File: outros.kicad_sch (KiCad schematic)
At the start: 9 parts

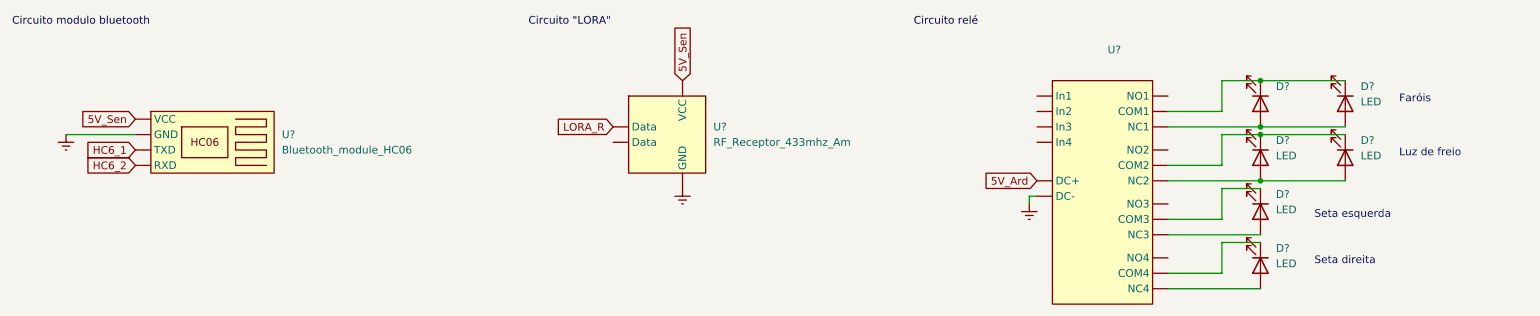
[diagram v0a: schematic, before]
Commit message: fix: modificado saídas do arduino
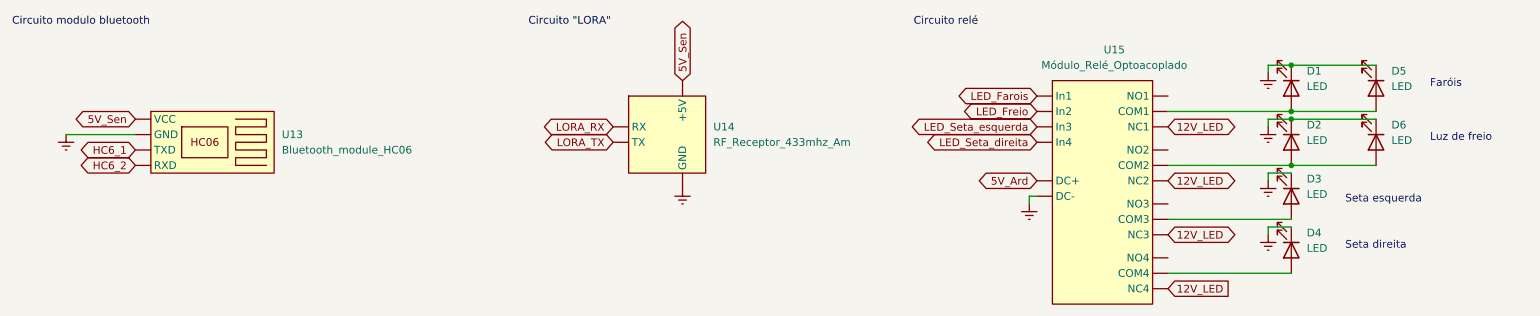
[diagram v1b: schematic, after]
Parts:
- D1: renamed from D?; value (none) -> LED
- U13: renamed from U?; footprint (none) -> Connector_PinHeader_2.54mm:PinHeader_1x04_P2.54mm_Vertical
- U14: renamed from U?; footprint (none) -> Connector_PinHeader_2.54mm:PinHeader_1x06_P2.54mm_Vertical; symbol Customizados:RF_Receptor_433mhz_Am -> Customizados:RF_Receptor_e_transmissor_915mhz
- U15: renamed from U?; value (none) -> Módulo_Relé_Optoacoplado; footprint (none) -> TerminalBlock_Phoenix:TerminalBlock_Phoenix_MKDS-1,5-6_1x06_P5.00mm_Horizontal
- gave numbers to parts that had none: 5
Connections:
- net LORA_R is gone; now on net LORA_TX: U14. (TX)
- net Earth: now also D1.1 (K), D2.1 (K), D3.1 (K), D4.1 (K), D5.1 (K), D6.1 (K)
- net LED_Seta_esquerda: now reaches U15. (NO4)
- net LORA_TX: now reaches U14. (TX)
- new net 12V_LED: U15. (NO4)
- new net LED_Farois: U15. (NO4)
- new net LED_Freio: U15. (NO4)
- new net LED_Seta_direita: U15. (NO4)
- new net LORA_RX: U14. (TX)
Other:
- moved on the sheet: D1, D2, D3, D4, D5, D6

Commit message: fix: mudanca dos pinos de alimentacao
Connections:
- net 5V_Ard: now also U13. (VCC); no longer U15. (NO4)
- net 5V_Sen: now also U15. (NO4); no longer U13. (VCC)
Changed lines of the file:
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@@
     )
   )
-  (global_label "5V_Ard" (shape bidirectional) (at 193.04 49.53 180) (fields_autoplaced)
+  (global_label "5V_Sen" (shape bidirectional) (at 193.04 49.53 180) (fields_autoplaced)
     (effects (font (size 1.27 1.27)) (justify right))
-    (property "Intersheetrefs" "${INTERSHEET_REFS}" (at 182.654 49.53 0)
+    (property "Intersheetrefs" "${INTERSHEET_REFS}" (at 182.2307 49.53 0)
       (effects (font (size 1.27 1.27)) (justify right))
     )
@@
     )
   )
-  (global_label "5V_Sen" (shape bidirectional) (at 44.45 39.37 180) (fields_autoplaced)
+  (global_label "5V_Ard" (shape bidirectional) (at 44.45 39.37 180) (fields_autoplaced)
     (effects (font (size 1.27 1.27)) (justify right))
-    (property "Intersheetrefs" "${INTERSHEET_REFS}" (at 33.6407 39.37 0)
+    (property "Intersheetrefs" "${INTERSHEET_REFS}" (at 34.064 39.37 0)
       (effects (font (size 1.27 1.27)) (justify right))
     )

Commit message: fix: esquematico atualizado
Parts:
- added D7, D8: LED, symbol Device:LED
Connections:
- net Earth: now also D7.1 (K), D8.1 (K)
- net at D3.2 (A), U15. (NO4): now also D7.2 (A)
- net at D4.2 (A), U15. (NO4): now also D8.2 (A)
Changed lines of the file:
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@@
   (junction (at 234.95 46.99) (diameter 0) (color 0 0 0 0)
   )
+  (junction (at 234.95 55.88) (diameter 0) (color 0 0 0 0)
+  )
+  (junction (at 234.95 48.26) (diameter 0) (color 0 0 0 0)
+  )
   (junction (at 234.95 30.48) (diameter 0) (color 0 0 0 0)
   )
+  (junction (at 234.95 57.15) (diameter 0) (color 0 0 0 0)
+  )
   (junction (at 234.95 39.37) (diameter 0) (color 0 0 0 0)
+  )
+  (junction (at 234.95 64.77) (diameter 0) (color 0 0 0 0)
   )
   (wire (pts (xy 214.63 64.77) (xy 234.95 64.77))
@@
     (stroke (width 0) (type default))
   )
+  (wire (pts (xy 234.95 57.15) (xy 248.92 57.15))
+    (stroke (width 0) (type default))
+  )
+  (wire (pts (xy 234.95 48.26) (xy 248.92 48.26))
+    (stroke (width 0) (type default))
+  )
   (wire (pts (xy 234.95 30.48) (xy 248.92 30.48))
     (stroke (width 0) (type default))
   )
+  (wire (pts (xy 234.95 64.77) (xy 248.92 64.77))
+    (stroke (width 0) (type default))
+  )
   (wire (pts (xy 33.02 41.91) (xy 44.45 41.91))
     (stroke (width 0) (type default))
@@
   )
   (wire (pts (xy 231.14 57.15) (xy 231.14 58.42))
+    (stroke (width 0) (type default))
+  )
+  (wire (pts (xy 234.95 55.88) (xy 248.92 55.88))
     (stroke (width 0) (type default))
   )
@@
     (effects (font (size 1.27 1.27)) (justify left bottom))
   )
-  (text "Seta direita\n" (at 243.84 60.96 0)
+  (text "Seta direita\n" (at 257.81 60.96 0)
     (effects (font (size 1.27 1.27)) (justify left bottom))
   )
-  (text "Seta esquerda\n" (at 243.84 53.34 0)
+  (text "Seta esquerda\n" (at 257.81 53.34 0)
     (effects (font (size 1.27 1.27)) (justify left bottom))
   )
@@
     )
   )
+  (symbol (lib_id "Device:LED") (at 248.92 52.07 270) (unit 1)
+    (in_bom yes) (on_board yes) (dnp no) (fields_autoplaced)
+    (property "Reference" "D7" (at 251.46 49.2124 90)
+      (effects (font (size 1.27 1.27)) (justify left))
+    )
+    (property "Value" "LED" (at 251.46 51.7524 90)
+      (effects (font (size 1.27 1.27)) (justify left))
+    )
+    (property "Footprint" "" (at 248.92 52.07 0)
+      (effects (font (size 1.27 1.27)) hide)
+    )
+    (property "Datasheet" "~" (at 248.92 52.07 0)
+      (effects (font (size 1.27 1.27)) hide)
+    )
+    (pin "1")
+    (pin "2")
+    (instances
+      (project "esquemaEletricoCarro"
+        (path "/e63e39d7-6ac0-4ffd-8aa3-1841a4541b55/4e8abd86-3528-401b-92d9-d0c0edaaa47f"
+          (reference "D7") (unit 1)
+        )
+      )
+    )
+  )
   (symbol (lib_id "Customizados:RF_Receptor_e_transmissor_915mhz") (at 132.08 41.91 0) (unit 1)
     (in_bom yes) (on_board yes) (dnp no) (fields_autoplaced)
@@
         )
       )
+    )
+  )
+  (symbol (lib_id "Device:LED") (at 248.92 60.96 270) (unit 1)
+    (in_bom yes) (on_board yes) (dnp no) (fields_autoplaced)
+    (property "Reference" "D8" (at 251.46 58.1024 90)
+      (effects (font (size 1.27 1.27)) (justify left))
+    )
+    (property "Value" "LED" (at 251.46 60.6424 90)
+      (effects (font (size 1.27 1.27)) (justify left))
+    )
+    (property "Footprint" "" (at 248.92 60.96 0)
+      (effects (font (size 1.27 1.27)) hide)
+    )
+    (property "Datasheet" "~" (at 248.92 60.96 0)
+      (effects (font (size 1.27 1.27)) hide)
+    )
+    (pin "1")
+    (pin "2")
+    (instances
+      (project "esquemaEletricoCarro"
+        (path "/e63e39d7-6ac0-4ffd-8aa3-1841a4541b55/4e8abd86-3528-401b-92d9-d0c0edaaa47f"
+          (reference "D8") (unit 1)
+        )
+      )
